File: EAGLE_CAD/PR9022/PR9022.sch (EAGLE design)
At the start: 70 parts, among them SW1 C&K_PTS645, U1 SI4702-C19-GMR, X1 ABS25XTAL

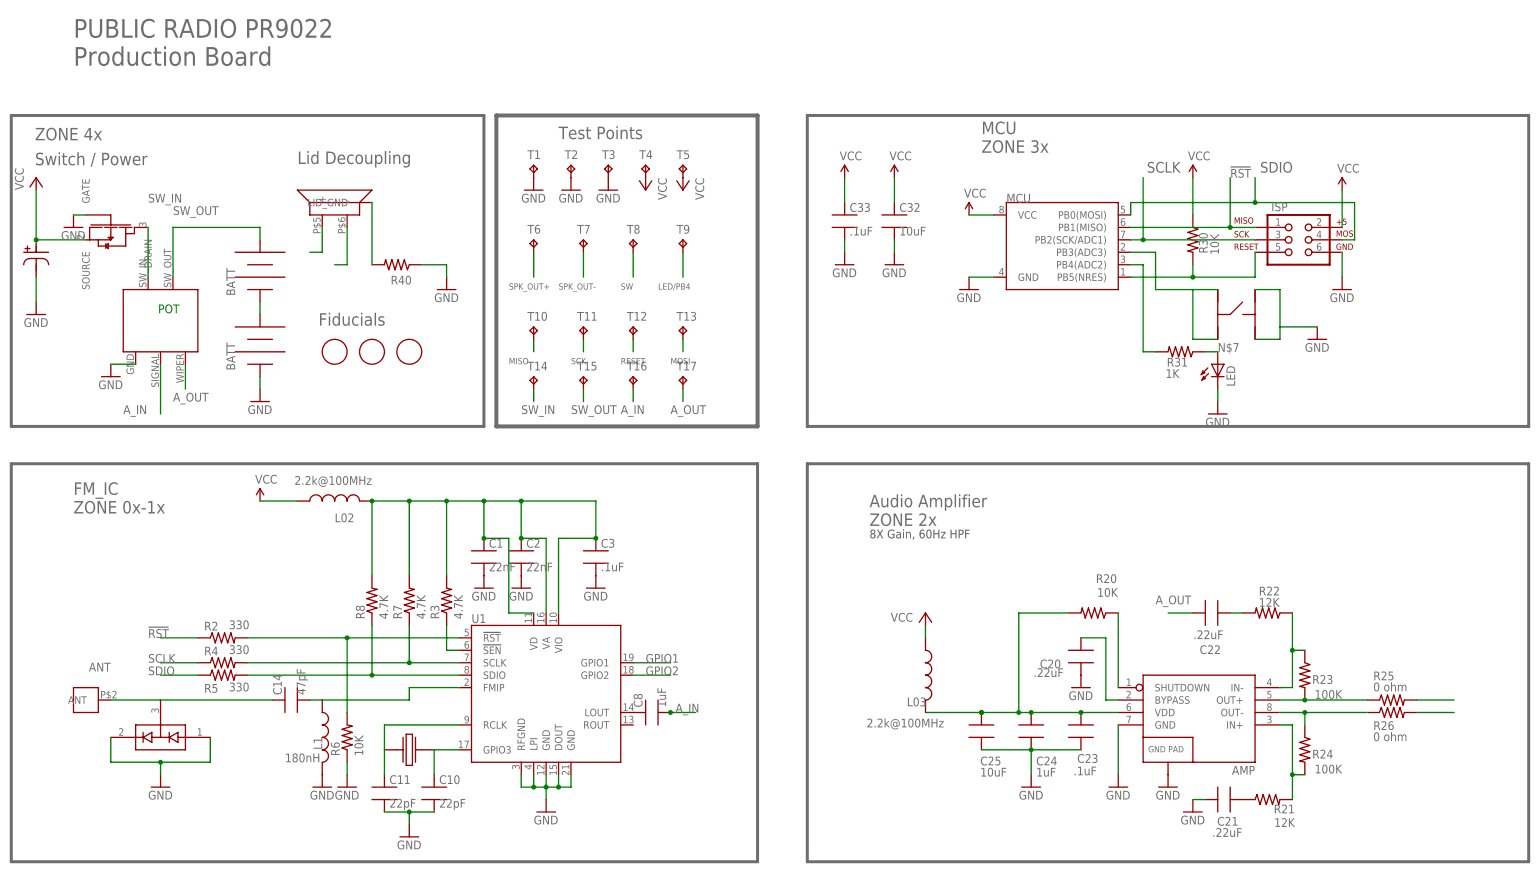
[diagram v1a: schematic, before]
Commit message: Small Changes
Updated the library to incorporate single M3_Pemnuts
Used these parts to build out the speaker connection points
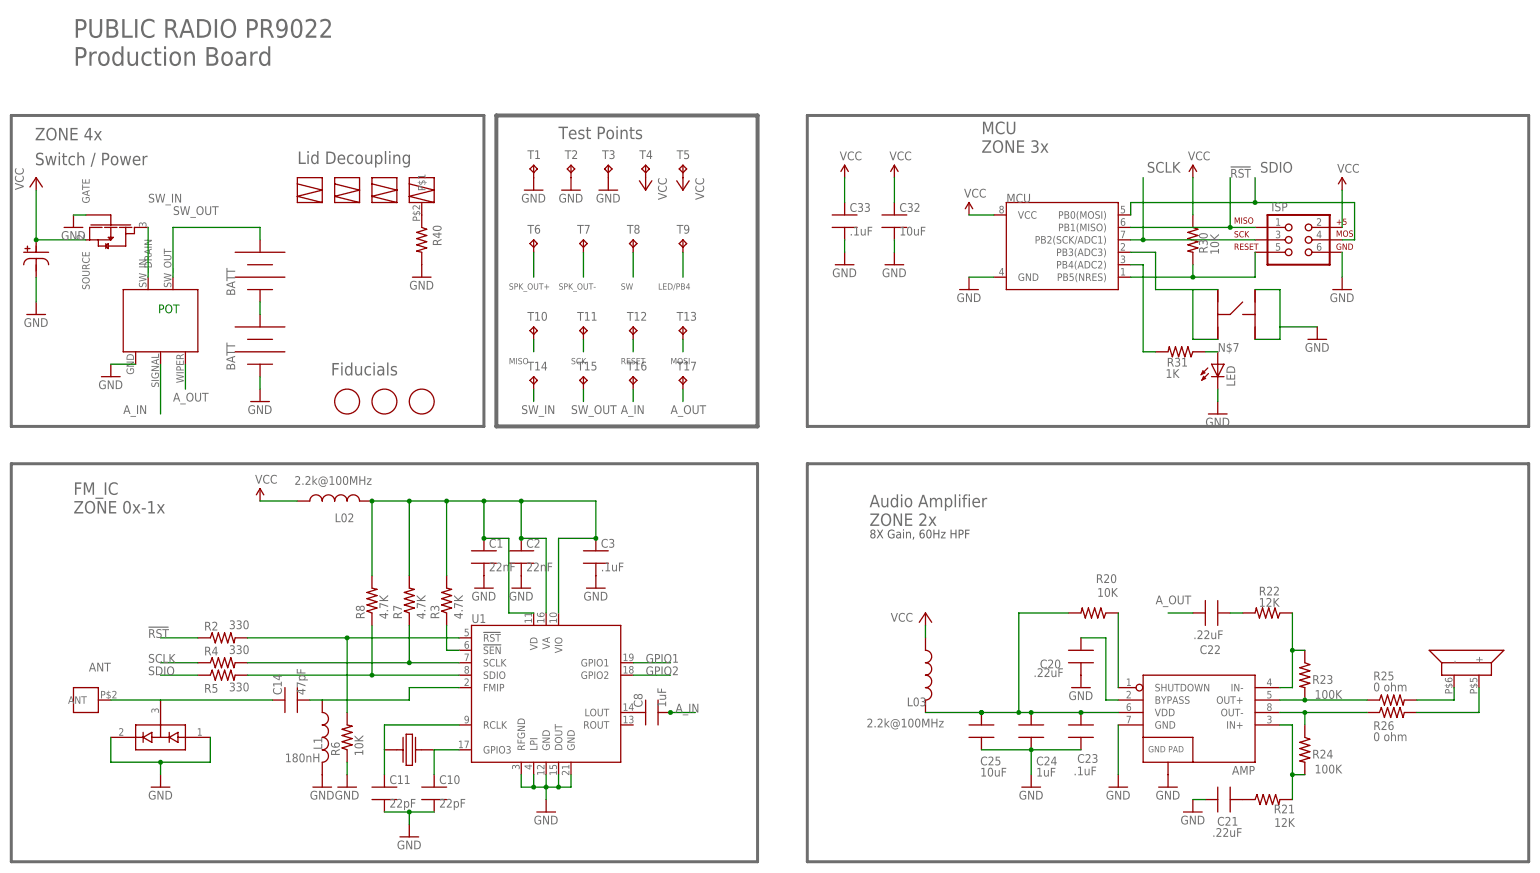
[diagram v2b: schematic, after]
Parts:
- added U$2, U$3, U$4: PEM_M3_NOPIN, PR_Parts_Library:PEM_M3_NOPIN
- added U$5: PEM_M3_W/PIN, PR_Parts_Library:PEM_M3_W/PIN
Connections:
- removed net N$8: R40.2, SPKR_PLACE.LID_GND
- new net N$6: R40.1, U$5.P$1
- net GND: now also R40.2; no longer R40.1
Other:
- moved on the sheet: R40
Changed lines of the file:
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@@
 <?xml version="1.0" encoding="utf-8"?>
 <!DOCTYPE eagle SYSTEM "eagle.dtd">
-<eagle version="7.2.0">
+<eagle version="6.6.0">
 <drawing>
 <settings>
@@
 <attribute name="MFG_PN" value="ERJ-6GEY0R00V "/>
 </part>
+<part name="U$2" library="PR_Parts_Library" deviceset="PEM_M3_NOPIN" device=""/>
+<part name="U$3" library="PR_Parts_Library" deviceset="PEM_M3_NOPIN" device=""/>
+<part name="U$4" library="PR_Parts_Library" deviceset="PEM_M3_NOPIN" device=""/>
+<part name="U$5" library="PR_Parts_Library" deviceset="PEM_M3_W/PIN" device=""/>
 </parts>
 <sheets>
@@
 <text x="-27.94" y="162.56" size="3.81" layer="96">PUBLIC RADIO PR9022
 Production Board </text>
-<text x="22.098" y="109.474" size="2.54" layer="96">Fiducials </text>
+<text x="24.638" y="99.314" size="2.54" layer="96">Fiducials </text>
 <text x="71.12" y="147.574" size="2.54" layer="96">Test Points </text>
 <text x="60.96" y="101.6" size="1.27" layer="95">MISO</text>
@@
 <instance part="GND20" gate="1" x="63.5" y="55.88"/>
 <instance part="GND9" gate="1" x="27.94" y="15.24"/>
-<instance part="SUPPLY5" gate="1" x="10.16" y="73.66"/>
+<instance part="SUPPLY5" gate="G$1" x="10.16" y="73.66"/>
 <instance part="R21" gate="G$1" x="215.9" y="12.7" smashed="yes">
 <attribute name="NAME" x="221.488" y="11.6586" size="1.778" layer="95" rot="R180"/>
@@
 <instance part="GND5" gate="1" x="-20.32" y="99.06"/>
 <instance part="GND2" gate="1" x="-35.56" y="111.76"/>
-<instance part="GND12" gate="1" x="48.26" y="116.84"/>
+<instance part="GND12" gate="1" x="43.18" y="119.38"/>
 <instance part="GND3" gate="1" x="-27.94" y="129.54"/>
 <instance part="MCU" gate="G$1" x="175.26" y="124.46"/>
-<instance part="SUPPLY8" gate="1" x="154.94" y="132.08"/>
+<instance part="SUPPLY8" gate="G$1" x="154.94" y="132.08"/>
 <instance part="GND25" gate="1" x="154.94" y="116.84"/>
 <instance part="GND23" gate="1" x="139.7" y="121.92"/>
 <instance part="GND22" gate="1" x="129.54" y="121.92"/>
-<instance part="SUPPLY6" gate="1" x="129.54" y="139.7"/>
-<instance part="SUPPLY7" gate="1" x="139.7" y="139.7"/>
+<instance part="SUPPLY6" gate="G$1" x="129.54" y="139.7"/>
+<instance part="SUPPLY7" gate="G$1" x="139.7" y="139.7"/>
 <instance part="GND31" gate="1" x="226.06" y="106.68"/>
 <instance part="ISP" gate="G$1" x="220.98" y="127"/>
 <instance part="GND30" gate="1" x="205.74" y="91.44"/>
-<instance part="SUPPLY9" gate="1" x="231.14" y="137.16"/>
+<instance part="SUPPLY9" gate="G$1" x="231.14" y="137.16"/>
 <instance part="GND32" gate="1" x="231.14" y="116.84"/>
 <instance part="R31" gate="G$1" x="198.12" y="104.14" smashed="yes" rot="R180">
@@
 <attribute name="VALUE" x="176.276" y="17.653" size="1.778" layer="96"/>
 </instance>
-<instance part="R40" gate="G$1" x="38.1" y="121.92" smashed="yes" rot="R180">
-<attribute name="NAME" x="36.83" y="117.8814" size="1.778" layer="95"/>
+<instance part="R40" gate="G$1" x="43.18" y="127" smashed="yes" rot="R270">
+<attribute name="NAME" x="47.2186" y="125.73" size="1.778" layer="95" rot="R90"/>
 </instance>
 <instance part="D1" gate="G$1" x="-10.16" y="25.4" rot="R180"/>
@@
 <attribute name="VALUE" x="205.994" y="123.952" size="1.778" layer="96" rot="R90"/>
 </instance>
-<instance part="SUPPLY1" gate="1" x="200.66" y="139.7"/>
+<instance part="SUPPLY1" gate="G$1" x="200.66" y="139.7"/>
 <instance part="C14" gate="G$1" x="15.24" y="33.02" rot="R90"/>
 <instance part="C11" gate="G$1" x="35.56" y="15.24"/>
@@
 <instance part="T12" gate="G$1" x="86.36" y="109.22"/>
 <instance part="T13" gate="G$1" x="96.52" y="109.22"/>
-<instance part="MARK1" gate="G$1" x="25.4" y="104.14"/>
-<instance part="MARK2" gate="G$1" x="33.02" y="104.14"/>
-<instance part="MARK3" gate="G$1" x="40.64" y="104.14"/>
+<instance part="MARK1" gate="G$1" x="27.94" y="93.98"/>
+<instance part="MARK2" gate="G$1" x="35.56" y="93.98"/>
+<instance part="MARK3" gate="G$1" x="43.18" y="93.98"/>
 <instance part="X1" gate="G$1" x="40.64" y="22.86" rot="R270"/>
 <instance part="C25" gate="G$1" x="157.48" y="27.94" smashed="yes">
@@
 <instance part="C8" gate="G$1" x="88.9" y="30.48" rot="R90"/>
 <instance part="FET1" gate="G$1" x="-20.32" y="129.54" rot="R270"/>
-<instance part="SPKR_PLACE" gate="G$1" x="25.4" y="134.62" rot="R90"/>
+<instance part="SPKR_PLACE" gate="G$1" x="256.54" y="40.64" rot="R90"/>
 <instance part="T14" gate="G$1" x="66.04" y="99.06"/>
 <instance part="T15" gate="G$1" x="76.2" y="99.06"/>
@@
 <attribute name="VALUE" x="237.49" y="24.638" size="1.778" layer="96"/>
 </instance>
+<instance part="U$2" gate="G$1" x="20.32" y="137.16"/>
+<instance part="U$3" gate="G$1" x="27.94" y="137.16"/>
+<instance part="U$4" gate="G$1" x="35.56" y="137.16"/>
+<instance part="U$5" gate="G$1" x="43.18" y="137.16"/>
 </instances>
 <busses>
@@
 </segment>
 <segment>
-<pinref part="R40" gate="G$1" pin="1"/>
-<pinref part="GND12" gate="1" pin="GND"/>
-<wire x1="43.18" y1="121.92" x2="48.26" y2="121.92" width="0.1524" layer="91"/>
-<wire x1="48.26" y1="121.92" x2="48.26" y2="119.38" width="0.1524" layer="91"/>
-</segment>
-<segment>
 <pinref part="AMP" gate="G$1" pin="GND@2"/>
 <pinref part="GND18" gate="1" pin="GND"/>
@@
 <pinref part="C3" gate="G$1" pin="2"/>
 <pinref part="GND17" gate="1" pin="GND"/>
+</segment>
+<segment>
+<pinref part="GND12" gate="1" pin="GND"/>
+<pinref part="R40" gate="G$1" pin="2"/>
 </segment>
 </net>
@@
 <segment>
 <pinref part="MCU" gate="G$1" pin="VCC"/>
-<pinref part="SUPPLY8" gate="1" pin="VCC"/>
+<pinref part="SUPPLY8" gate="G$1" pin="VCC"/>
 <wire x1="160.02" y1="132.08" x2="154.94" y2="132.08" width="0.1524" layer="91"/>
 </segment>
 <segment>
 <pinref part="L02" gate="G$1" pin="1"/>
-<pinref part="SUPPLY5" gate="1" pin="VCC"/>
+<pinref part="SUPPLY5" gate="G$1" pin="VCC"/>
 <wire x1="17.78" y1="73.66" x2="10.16" y2="73.66" width="0.1524" layer="91"/>
 </segment>
@@
 <pinref part="ISP" gate="G$1" pin="2"/>
 <wire x1="231.14" y1="137.16" x2="231.14" y2="129.54" width="0.1524" layer="91"/>
-<pinref part="SUPPLY9" gate="1" pin="VCC"/>
-</segment>
-<segment>
-<pinref part="SUPPLY6" gate="1" pin="VCC"/>
+<pinref part="SUPPLY9" gate="G$1" pin="VCC"/>
+</segment>
+<segment>
+<pinref part="SUPPLY6" gate="G$1" pin="VCC"/>
 <pinref part="C33" gate="G$1" pin="1"/>
 <wire x1="129.54" y1="139.7" x2="129.54" y2="134.62" width="0.1524" layer="91"/>
 </segment>
 <segment>
-<pinref part="SUPPLY7" gate="1" pin="VCC"/>
+<pinref part="SUPPLY7" gate="G$1" pin="VCC"/>
 <wire x1="139.7" y1="139.7" x2="139.7" y2="134.62" width="0.1524" layer="91"/>
 <pinref part="C32" gate="G$1" pin="1"/>
@@
 <pinref part="R30" gate="G$1" pin="1"/>
 <wire x1="200.66" y1="132.08" x2="200.66" y2="139.7" width="0.1524" layer="91"/>
-<pinref part="SUPPLY1" gate="1" pin="VCC"/>
+<pinref part="SUPPLY1" gate="G$1" pin="VCC"/>
 </segment>
 <segment>
@@
 <wire x1="246.38" y1="33.02" x2="254" y2="33.02" width="0.1524" layer="91"/>
 <pinref part="R25" gate="G$1" pin="2"/>
-</segment>
-<segment>
 <pinref part="SPKR_PLACE" gate="G$1" pin="-"/>
-<wire x1="27.94" y1="129.54" x2="27.94" y2="121.92" width="0.1524" layer="91"/>
-<wire x1="27.94" y1="121.92" x2="25.4" y2="121.92" width="0.1524" layer="91"/>
+<wire x1="254" y1="33.02" x2="254" y2="35.56" width="0.1524" layer="91"/>
 </segment>
 </net>
@@
 </segment>
 <segment>
-<wire x1="246.38" y1="30.48" x2="254" y2="30.48" width="0.1524" layer="91"/>
 <pinref part="R26" gate="G$1" pin="2"/>
-</segment>
-<segment>
 <pinref part="SPKR_PLACE" gate="G$1" pin="+"/>
-<wire x1="22.86" y1="129.54" x2="22.86" y2="124.46" width="0.1524" layer="91"/>
-<wire x1="22.86" y1="124.46" x2="20.32" y2="124.46" width="0.1524" layer="91"/>
+<wire x1="246.38" y1="30.48" x2="259.08" y2="30.48" width="0.1524" layer="91"/>
+<wire x1="259.08" y1="30.48" x2="259.08" y2="35.56" width="0.1524" layer="91"/>
 </segment>
 </net>
@@
 <pinref part="U1" gate="G$1" pin="LOUT"/>
 <pinref part="C8" gate="G$1" pin="1"/>
-</segment>
-</net>
-<net name="N$8" class="0">
-<segment>
-<pinref part="SPKR_PLACE" gate="G$1" pin="LID_GND"/>
-<pinref part="R40" gate="G$1" pin="2"/>
-<wire x1="33.02" y1="134.62" x2="33.02" y2="121.92" width="0.1524" layer="91"/>
 </segment>
 </net>
@@
 </segment>
 </net>
+<net name="N$6" class="0">
+<segment>
+<pinref part="R40" gate="G$1" pin="1"/>
+<pinref part="U$5" gate="G$1" pin="P$1"/>
+</segment>
+</net>
